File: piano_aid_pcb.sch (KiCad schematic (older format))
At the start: 15 parts

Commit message: Added screw terminal and power regulation
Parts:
- added C?: 10µ, symbol Device:CP1
- added C?: 22µ, symbol Device:CP1
- added J?: Screw_Terminal_01x02, symbol Connector:Screw_Terminal_01x02
- added U?: AZ1117-3.3, symbol Regulator_Linear:AZ1117-3.3
- C?: value CP1 -> 1000µ
- U?: symbol 317030213:317030213 -> piano_aid_pcb-rescue:317030213-317030213
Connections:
- net 3.3V: now also C?.1, U?.2 (VO)
- net 5V: now also J?.1 (Pin_1)
- net GND: now also C?.1, C?.2, C?.2, J?.2 (Pin_2), U?.1 (GND), U?.3 (VI)
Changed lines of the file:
@@
 $EndDescr
 $Comp
-L 317030213:317030213 U?
+L piano_aid_pcb-rescue:317030213-317030213 U?
 U 1 1 6137BBB1
 P 4650 3700
@@
 P 1650 1000
 F 0 "C?" H 1765 1046 50  0000 L CNN
-F 1 "CP1" H 1765 955 50  0000 L CNN
+F 1 "1000µ" H 1765 955 50  0000 L CNN
 F 2 "" H 1650 1000 50  0001 C CNN
 F 3 "~" H 1650 1000 50  0001 C CNN
@@
 Wire Wire Line
 	1200 3100 2000 3100
-Text GLabel 2300 850  2    50   Input ~ 0
+Text GLabel 3000 850  2    50   Input ~ 0
 5V
-Text GLabel 2300 1150 2    50   Input ~ 0
-GND
-Wire Wire Line
-	1650 1150 2300 1150
+Text GLabel 3000 1150 2    50   Input ~ 0
+GND
 Connection ~ 1650 1150
-Wire Wire Line
-	1650 850  2300 850
 Connection ~ 1650 850
 Text GLabel 9250 800  1    50   Input ~ 0
@@
 Wire Wire Line
 	8300 4500 8900 4500
+$Comp
+L Regulator_Linear:AZ1117-3.3 U?
+U 1 1 6144F069
+P 1800 2050
+F 0 "U?" H 1800 2199 50  0000 C CNN
+F 1 "AZ1117-3.3" H 1800 2290 50  0000 C CNN
+F 2 "" H 1800 2300 50  0001 C CIN
+F 3 "https://www.diodes.com/assets/Datasheets/AZ1117.pdf" H 1800 2050 50  0001 C CNN
+	1    1800 2050
+	-1   0    0    1
+$EndComp
+Wire Wire Line
+	1650 1150 1800 1150
+Connection ~ 1800 1150
+Wire Wire Line
+	1800 1150 2100 1150
+Connection ~ 2100 1150
+$Comp
+L Device:CP1 C?
+U 1 1 61457074
+P 1950 1550
+F 0 "C?" V 1698 1550 50  0000 C CNN
+F 1 "10µ" V 1789 1550 50  0000 C CNN
+F 2 "" H 1950 1550 50  0001 C CNN
+F 3 "~" H 1950 1550 50  0001 C CNN
+	1    1950 1550
+	0    1    1    0
+$EndComp
+$Comp
+L Device:CP1 C?
+U 1 1 6145E06D
+P 1650 1550
+F 0 "C?" V 1902 1550 50  0000 C CNN
+F 1 "22µ" V 1811 1550 50  0000 C CNN
+F 2 "" H 1650 1550 50  0001 C CNN
+F 3 "~" H 1650 1550 50  0001 C CNN
+	1    1650 1550
+	0    -1   -1   0
+$EndComp
+Connection ~ 2100 1550
+Wire Wire Line
+	2100 1550 2100 2050
+Connection ~ 1800 1550
+Wire Wire Line
+	1800 1550 1800 1750
+Wire Wire Line
+	1500 1550 1500 2050
+Wire Wire Line
+	2100 1150 2100 1550
+Wire Wire Line
+	1800 1150 1800 1550
+Wire Wire Line
+	1500 1550 1200 1550
+Connection ~ 1500 1550
+Text GLabel 1200 1550 0    50   Input ~ 0
+3.3V
+$Comp
+L Connector:Screw_Terminal_01x02 J?
+U 1 1 61467FBD
+P 2600 600
+F 0 "J?" V 2564 412 50  0000 R CNN
+F 1 "Screw_Terminal_01x02" V 2473 412 50  0000 R CNN
+F 2 "" H 2600 600 50  0001 C CNN
+F 3 "~" H 2600 600 50  0001 C CNN
+	1    2600 600
+	0    -1   -1   0
+$EndComp
+Wire Wire Line
+	2600 850  2600 800
+Wire Wire Line
+	1650 850  2600 850
+Wire Wire Line
+	2600 850  3000 850
+Connection ~ 2600 850
+Wire Wire Line
+	2700 800  2700 1150
+Wire Wire Line
+	2700 1150 3000 1150
+Wire Wire Line
+	2100 1150 2700 1150
+Connection ~ 2700 1150
 $EndSCHEMATC

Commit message: Added more connections
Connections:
- net GND: now also U?.1
- net MIDI_DIN: now reaches U?.21 (P0.08)
- net MIDI_DIN: now also R?.2, U?.6 (VO2)
- net at U?.31 (P0.17): now also U?.2
- net at U?.4: now also R?.2
- net LED_DIN: now reaches R?.1
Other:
- moved on the sheet: R?, U?
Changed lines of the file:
@@
 L 74xGxx:74AHCT1G125 U?
 U 1 1 6138B78A
-P 1050 6300
-F 0 "U?" H 1025 6125 50  0000 C CNN
-F 1 "74AHCT1G125" H 1025 6034 50  0000 C CNN
-F 2 "" H 1050 6300 50  0001 C CNN
-F 3 "http://www.ti.com/lit/sg/scyt129e/scyt129e.pdf" H 1050 6300 50  0001 C CNN
-	1    1050 6300
+P 7950 2800
+F 0 "U?" H 7925 2625 50  0000 C CNN
+F 1 "74AHCT1G125" H 7925 2534 50  0000 C CNN
+F 2 "" H 7950 2800 50  0001 C CNN
+F 3 "http://www.ti.com/lit/sg/scyt129e/scyt129e.pdf" H 7950 2800 50  0001 C CNN
+	1    7950 2800
 	1    0    0    -1
 $EndComp
@@
 L Device:R R?
 U 1 1 6139F900
-P 1650 6300
-F 0 "R?" V 1443 6300 50  0000 C CNN
-F 1 "440" V 1534 6300 50  0000 C CNN
-F 2 "" V 1580 6300 50  0001 C CNN
-F 3 "~" H 1650 6300 50  0001 C CNN
-	1    1650 6300
+P 8550 2800
+F 0 "R?" V 8343 2800 50  0000 C CNN
+F 1 "440" V 8434 2800 50  0000 C CNN
+F 2 "" V 8480 2800 50  0001 C CNN
+F 3 "~" H 8550 2800 50  0001 C CNN
+	1    8550 2800
 	0    1    1    0
 $EndComp
@@
 Wire Wire Line
 	5650 3700 6900 3700
-Wire Wire Line
-	6900 3700 6900 5150
 $Comp
 L Connector:Conn_01x06_Female J?
@@
 	-1   0    0    1
 $EndComp
-Wire Wire Line
-	2500 3300 1200 3300
-Wire Wire Line
-	2500 3300 2500 5150
 Text Label 1250 2800 0    50   ~ 0
 VDD
@@
 	9250 4300 9150 4300
 Wire Wire Line
-	2500 5150 6900 5150
-Wire Wire Line
 	8650 4000 9250 4000
 Wire Wire Line
@@
 	2100 1150 2700 1150
 Connection ~ 2700 1150
+Text GLabel 7950 2400 1    50   Input ~ 0
+GND
+Wire Wire Line
+	7950 2600 7950 2400
+Wire Wire Line
+	5650 3300 6900 3300
+Wire Wire Line
+	6900 3300 6900 2800
+Wire Wire Line
+	6900 2800 7650 2800
+Wire Wire Line
+	8200 2800 8400 2800
+Wire Wire Line
+	8700 2800 9250 2800
+Text GLabel 9250 2800 2    50   Input ~ 0
+LED_DIN
+Text GLabel 6900 3700 2    50   Input ~ 0
+RESET
+Text GLabel 2000 3300 2    50   Input ~ 0
+RESET
+Wire Wire Line
+	1200 3300 2000 3300
+Text GLabel 10100 1450 2    50   Input ~ 0
+MIDI_DIN
+Text GLabel 3150 4000 0    50   Input ~ 0
+MIDI_DIN
+Wire Wire Line
+	3150 4000 3650 4000
 $EndSCHEMATC

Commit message: Added more caps
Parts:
- added C?: 0.1µ, symbol Device:CP1
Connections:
- net 5V: now also C?.1
- net GND: now also C?.2
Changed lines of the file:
@@
 	2600 850  2600 800
 Wire Wire Line
-	1650 850  2600 850
+	1650 850  2250 850
 Wire Wire Line
 	2600 850  3000 850
@@
 	2700 1150 3000 1150
 Wire Wire Line
-	2100 1150 2700 1150
+	2100 1150 2250 1150
 Connection ~ 2700 1150
 Text GLabel 7950 2400 1    50   Input ~ 0
@@
 Wire Wire Line
 	3150 4000 3650 4000
+$Comp
+L Device:CP1 C?
+U 1 1 61480AF3
+P 2250 1000
+F 0 "C?" H 2365 1046 50  0000 L CNN
+F 1 "0.1µ" H 2365 955 50  0000 L CNN
+F 2 "" H 2250 1000 50  0001 C CNN
+F 3 "~" H 2250 1000 50  0001 C CNN
+	1    2250 1000
+	1    0    0    -1
+$EndComp
+Connection ~ 2250 850
+Wire Wire Line
+	2250 850  2600 850
+Connection ~ 2250 1150
+Wire Wire Line
+	2250 1150 2700 1150
 $EndSCHEMATC

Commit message: Added power supply to logic level converter
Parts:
- added C?: 0.1µ, symbol Device:CP1
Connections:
- net 5V is gone; now on net VCC: C?.1, C?.1, C?.1, J?.1, J?.1 (Pin_1), U?.8 (VCC)
- net GND: now also C?.2
- net at J?.2: now also C?.1
- no-connect marks 5 -> 4
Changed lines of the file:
@@
 NoConn ~ 6600 1000
 NoConn ~ 6600 1900
-NoConn ~ 7050 1450
-Wire Wire Line
-	6900 1450 7050 1450
 Wire Wire Line
 	6600 1150 6600 1000
@@
 Wire Wire Line
 	2250 1150 2700 1150
+Wire Wire Line
+	7250 1450 7250 1750
+Wire Wire Line
+	6900 1450 7250 1450
+$Comp
+L Device:CP1 C?
+U 1 1 6148405B
+P 7250 1900
+F 0 "C?" H 7365 1946 50  0000 L CNN
+F 1 "0.1µ" H 7365 1855 50  0000 L CNN
+F 2 "" H 7250 1900 50  0001 C CNN
+F 3 "~" H 7250 1900 50  0001 C CNN
+	1    7250 1900
+	1    0    0    -1
+$EndComp
+Text GLabel 7250 2050 3    50   Input ~ 0
+GND
+Wire Wire Line
+	8000 2850 8000 2950
+Wire Wire Line
+	8000 2950 8300 2950
+Wire Wire Line
+	8300 2950 8300 3250
+Wire Wire Line
+	8000 2750 8000 2650
+Wire Wire Line
+	8000 2650 8300 2650
+Wire Wire Line
+	8300 2650 8300 2400
+Text GLabel 8300 3250 3    50   Input ~ 0
+GND
+Text GLabel 8300 2400 1    50   Input ~ 0
+5V
 $EndSCHEMATC

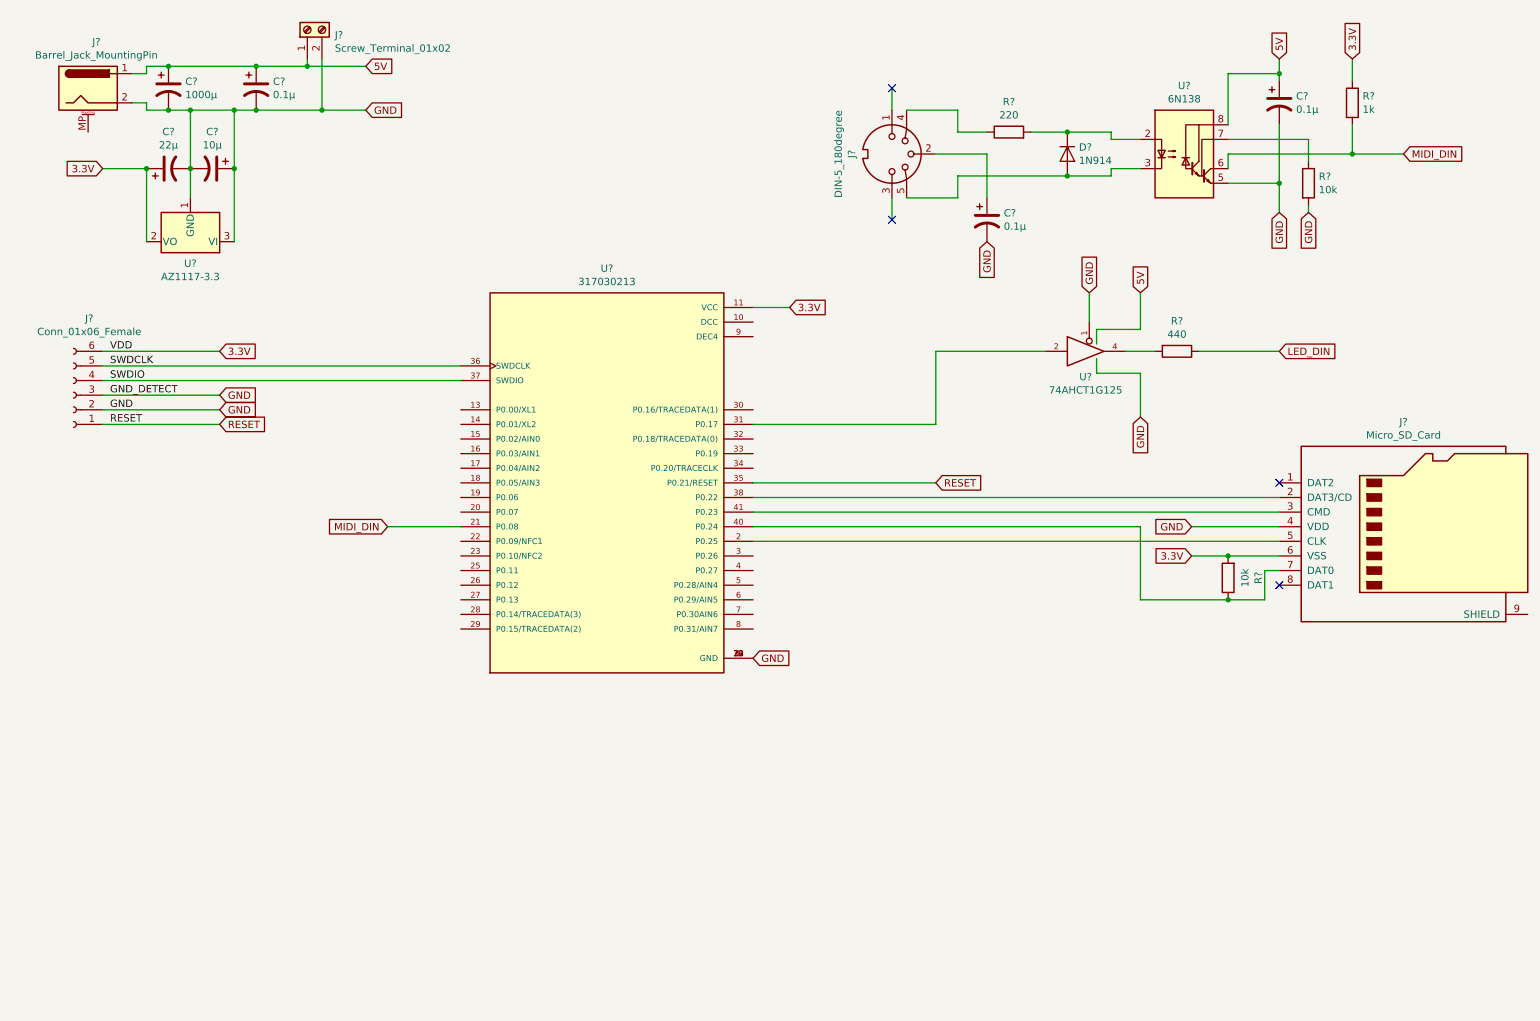
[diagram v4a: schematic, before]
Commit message: Updated MIDI-DIN
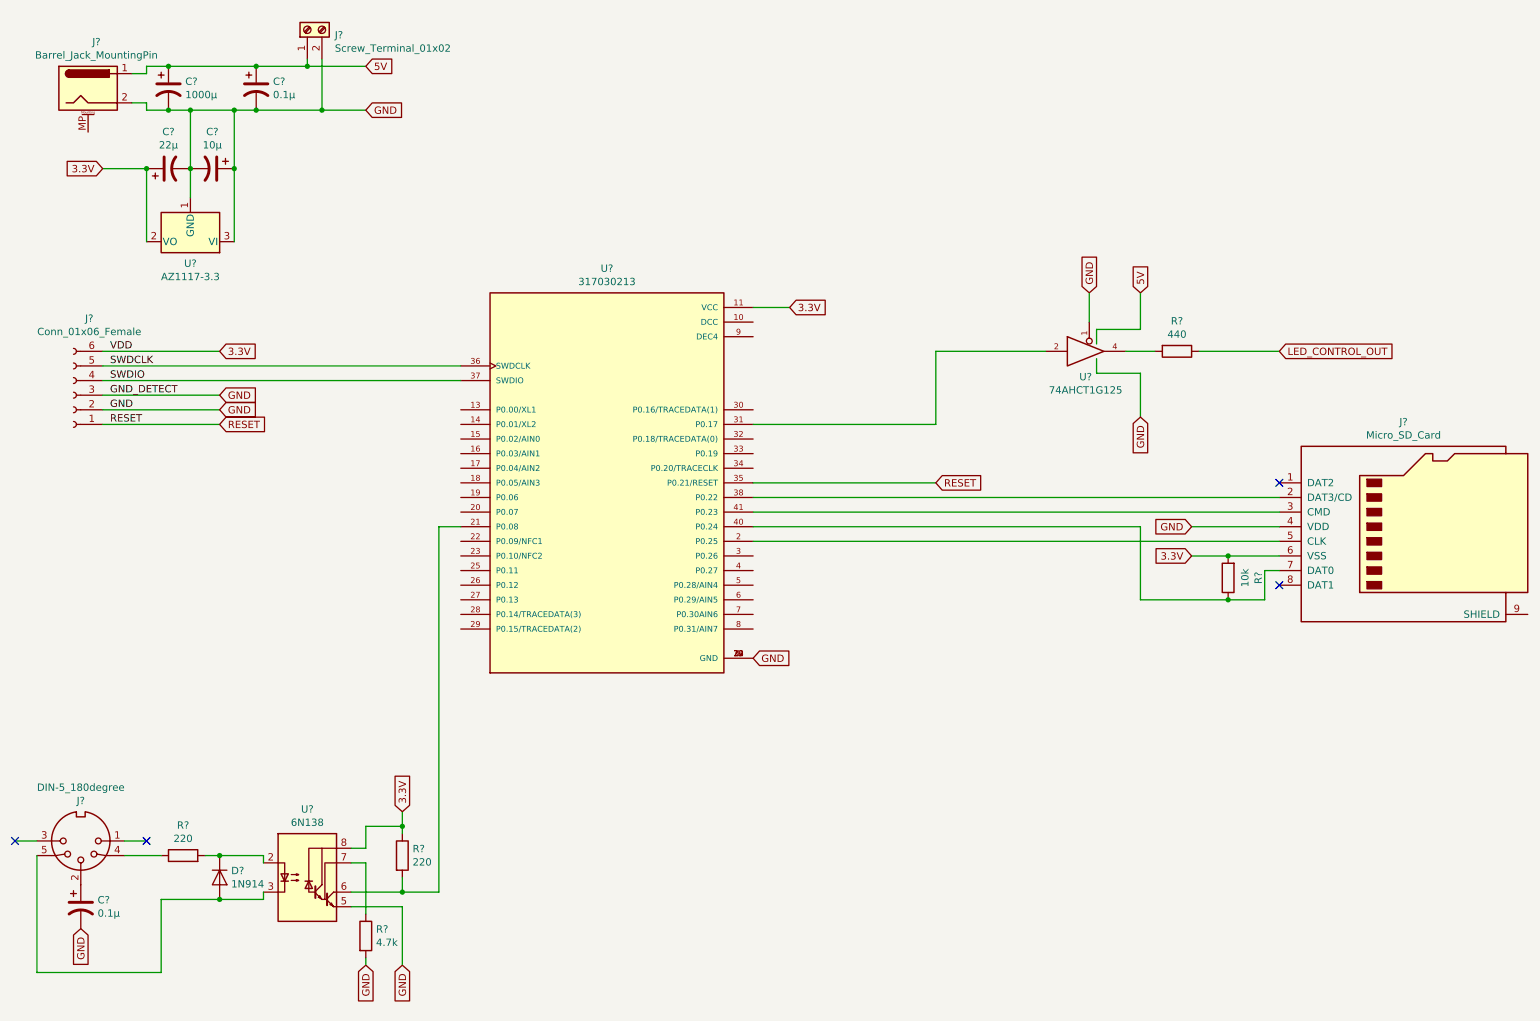
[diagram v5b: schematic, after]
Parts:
- removed C?: 0.1µ, symbol Device:CP1
- removed R?: 1k, symbol Device:R
- added R?: 220, symbol Device:R
- R?: value 10k -> 4.7k
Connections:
- net 3.3V: now also U?.8 (VCC), R?.1
- net VCC: no longer U?.8 (VCC)
- net LED_DIN renamed LED_CONTROL_OUT
- net MIDI_DIN: no longer names the net of U?.21 (P0.08), U?.6 (VO2)
- net MIDI_DIN: now also R?.2
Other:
- moved on the sheet: C?, D?, J?, R?, U?
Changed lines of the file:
@@
-$EndComp
-$Comp
-L Connector:DIN-5_180degree J?
-U 1 1 61399AC9
-P 6600 1450
-F 0 "J?" H 6600 1175 50  0000 C CNN
-F 1 "DIN-5_180degree" H 6600 1084 50  0000 C CNN
-F 2 "" H 6600 1450 50  0001 C CNN
-F 3 "http://www.mouser.com/ds/2/18/40_c091_abd_e-75918.pdf" H 6600 1450 50  0001 C CNN
-	1    6600 1450
-	0    1    1    0
 $EndComp
 $Comp
@@
 Wire Wire Line
 	1500 1150 1650 1150
-$Comp
-L Diode:1N914 D?
-U 1 1 613A3625
-P 7800 1450
-F 0 "D?" V 7754 1529 50  0000 L CNN
-F 1 "1N914" V 7845 1529 50  0000 L CNN
-F 2 "Diode_THT:D_DO-35_SOD27_P7.62mm_Horizontal" H 7800 1275 50  0001 C CNN
-F 3 "http://www.vishay.com/docs/85622/1n914.pdf" H 7800 1450 50  0001 C CNN
-	1    7800 1450
-	0    1    1    0
-$EndComp
-$Comp
-L Device:R R?
-U 1 1 613ABD6D
-P 7400 1300
-F 0 "R?" V 7607 1300 50  0000 C CNN
-F 1 "220" V 7516 1300 50  0000 C CNN
-F 2 "" V 7330 1300 50  0001 C CNN
-F 3 "~" H 7400 1300 50  0001 C CNN
-	1    7400 1300
-	0    -1   -1   0
-$EndComp
-$Comp
-L Isolator:6N138 U?
-U 1 1 613CE47C
-P 8600 1450
-F 0 "U?" H 8600 1917 50  0000 C CNN
-F 1 "6N138" H 8600 1826 50  0000 C CNN
-F 2 "" H 8890 1150 50  0001 C CNN
-F 3 "http://www.onsemi.com/pub/Collateral/HCPL2731-D.pdf" H 8890 1150 50  0001 C CNN
-	1    8600 1450
-	1    0    0    -1
-$EndComp
 Wire Wire Line
 	1200 2900 3650 2900
@@
 $EndComp
 Wire Wire Line
-	6700 1150 7050 1150
-Wire Wire Line
-	7050 1150 7050 1300
-Wire Wire Line
-	7050 1300 7250 1300
-Wire Wire Line
-	7550 1300 7800 1300
-Wire Wire Line
-	7800 1300 8100 1300
-Wire Wire Line
-	8100 1300 8100 1350
-Wire Wire Line
-	8100 1350 8300 1350
-Connection ~ 7800 1300
-Wire Wire Line
-	7800 1600 8100 1600
-Wire Wire Line
-	8100 1600 8100 1550
-Wire Wire Line
-	8100 1550 8300 1550
-Wire Wire Line
-	6700 1750 7050 1750
-Wire Wire Line
-	7050 1750 7050 1600
-Wire Wire Line
-	7050 1600 7800 1600
-Connection ~ 7800 1600
-$Comp
-L Device:CP1 C?
-U 1 1 6142C582
-P 9250 1100
-F 0 "C?" H 9365 1146 50  0000 L CNN
-F 1 "0.1µ" H 9365 1055 50  0000 L CNN
-F 2 "" H 9250 1100 50  0001 C CNN
-F 3 "~" H 9250 1100 50  0001 C CNN
-	1    9250 1100
-	1    0    0    -1
-$EndComp
-Wire Wire Line
-	8900 1250 8900 900
-Wire Wire Line
-	8900 900  9250 900
-Wire Wire Line
-	9250 900  9250 800
-Wire Wire Line
-	9250 950  9250 900
-Connection ~ 9250 900
-Wire Wire Line
-	8900 1650 9250 1650
-Wire Wire Line
-	9250 1650 9250 1250
-Wire Wire Line
-	9250 1850 9250 1650
-Connection ~ 9250 1650
-$Comp
-L Device:R R?
-U 1 1 61445BFE
-P 9450 1650
-F 0 "R?" H 9520 1696 50  0000 L CNN
-F 1 "10k" H 9520 1605 50  0000 L CNN
-F 2 "" V 9380 1650 50  0001 C CNN
-F 3 "~" H 9450 1650 50  0001 C CNN
-	1    9450 1650
-	1    0    0    -1
-$EndComp
-Wire Wire Line
-	9450 1800 9450 1850
-Wire Wire Line
-	8900 1350 9450 1350
-Wire Wire Line
-	9450 1350 9450 1500
-Wire Wire Line
-	8900 1550 8900 1450
-Wire Wire Line
-	8900 1450 9750 1450
-$Comp
-L Device:R R?
-U 1 1 6144C0EE
-P 9750 1100
-F 0 "R?" H 9820 1146 50  0000 L CNN
-F 1 "1k" H 9820 1055 50  0000 L CNN
-F 2 "" V 9680 1100 50  0001 C CNN
-F 3 "~" H 9750 1100 50  0001 C CNN
-	1    9750 1100
-	1    0    0    -1
-$EndComp
-Wire Wire Line
-	9750 800  9750 950
-Wire Wire Line
-	9750 1250 9750 1450
-Connection ~ 9750 1450
-Wire Wire Line
-	9750 1450 10100 1450
-Wire Wire Line
 	1200 3100 2000 3100
 Text GLabel 3000 850  2    50   Input ~ 0
@@
 Connection ~ 1650 1150
 Connection ~ 1650 850
-Text GLabel 9250 800  1    50   Input ~ 0
-5V
-Text GLabel 9750 800  1    50   Input ~ 0
-3.3V
-Text GLabel 9250 1850 3    50   Input ~ 0
-GND
-Text GLabel 9450 1850 3    50   Input ~ 0
-GND
 Text GLabel 8650 4200 0    50   Input ~ 0
 3.3V
@@
 	8650 4200 8900 4200
 Connection ~ 8900 4200
-NoConn ~ 6600 1000
-NoConn ~ 6600 1900
-Wire Wire Line
-	6600 1150 6600 1000
-Wire Wire Line
-	6600 1750 6600 1900
 Wire Wire Line
 	9250 3800 5650 3800
@@
 	2100 1150 2250 1150
 Connection ~ 2700 1150
-Text GLabel 7950 2400 1    50   Input ~ 0
-GND
 Wire Wire Line
 	7950 2600 7950 2400
@@
 	8700 2800 9250 2800
 Text GLabel 9250 2800 2    50   Input ~ 0
-LED_DIN
+LED_CONTROL_OUT
 Text GLabel 6900 3700 2    50   Input ~ 0
 RESET
@@
 Wire Wire Line
 	1200 3300 2000 3300
-Text GLabel 10100 1450 2    50   Input ~ 0
-MIDI_DIN
-Text GLabel 3150 4000 0    50   Input ~ 0
-MIDI_DIN
-Wire Wire Line
-	3150 4000 3650 4000
 $Comp
 L Device:CP1 C?
@@
 	2250 1150 2700 1150
 Wire Wire Line
-	7250 1450 7250 1750
-Wire Wire Line
-	6900 1450 7250 1450
+	8000 2850 8000 2950
+Wire Wire Line
+	8000 2950 8300 2950
+Wire Wire Line
+	8300 2950 8300 3250
+Wire Wire Line
+	8000 2750 8000 2650
+Wire Wire Line
+	8000 2650 8300 2650
+Wire Wire Line
+	8300 2650 8300 2400
+Text GLabel 8300 3250 3    50   Input ~ 0
+GND
+Text GLabel 8300 2400 1    50   Input ~ 0
+5V
+Text GLabel 7950 2400 1    50   Input ~ 0
+GND
+Wire Wire Line
+	3650 4000 3500 4000
+Wire Wire Line
+	3500 4000 3500 6500
+Connection ~ 2000 6550
+Wire Wire Line
+	2000 6550 1600 6550
+Connection ~ 2000 6250
+Wire Wire Line
+	1900 6250 2000 6250
+Wire Wire Line
+	1350 6250 1600 6250
+$Comp
+L Connector:DIN-5_180degree J?
+U 1 1 61399AC9
+P 1050 6150
+F 0 "J?" H 1050 5875 50  0000 C CNN
+F 1 "DIN-5_180degree" H 1050 5784 50  0000 C CNN
+F 2 "" H 1050 6150 50  0001 C CNN
+F 3 "http://www.mouser.com/ds/2/18/40_c091_abd_e-75918.pdf" H 1050 6150 50  0001 C CNN
+	1    1050 6150
+	-1   0    0    1
+$EndComp
+$Comp
+L Diode:1N914 D?
+U 1 1 613A3625
+P 2000 6400
+F 0 "D?" V 1954 6479 50  0000 L CNN
+F 1 "1N914" V 2045 6479 50  0000 L CNN
+F 2 "Diode_THT:D_DO-35_SOD27_P7.62mm_Horizontal" H 2000 6225 50  0001 C CNN
+F 3 "http://www.vishay.com/docs/85622/1n914.pdf" H 2000 6400 50  0001 C CNN
+	1    2000 6400
+	0    1    1    0
+$EndComp
+Wire Wire Line
+	2000 6250 2300 6250
+Wire Wire Line
+	2300 6250 2300 6300
+Wire Wire Line
+	2000 6550 2300 6550
+Wire Wire Line
+	2300 6550 2300 6500
+$Comp
+L Device:R R?
+U 1 1 61445BFE
+P 3000 6800
+F 0 "R?" H 3070 6846 50  0000 L CNN
+F 1 "4.7k" H 3070 6755 50  0000 L CNN
+F 2 "" V 2930 6800 50  0001 C CNN
+F 3 "~" H 3000 6800 50  0001 C CNN
+	1    3000 6800
+	1    0    0    -1
+$EndComp
+Wire Wire Line
+	3000 6950 3000 7000
+Wire Wire Line
+	2900 6300 3000 6300
+Text GLabel 3250 5950 1    50   Input ~ 0
+3.3V
+Text GLabel 3250 7000 3    50   Input ~ 0
+GND
+Text GLabel 3000 7000 3    50   Input ~ 0
+GND
 $Comp
 L Device:CP1 C?
 U 1 1 6148405B
-P 7250 1900
-F 0 "C?" H 7365 1946 50  0000 L CNN
-F 1 "0.1µ" H 7365 1855 50  0000 L CNN
-F 2 "" H 7250 1900 50  0001 C CNN
-F 3 "~" H 7250 1900 50  0001 C CNN
-	1    7250 1900
-	1    0    0    -1
-$EndComp
-Text GLabel 7250 2050 3    50   Input ~ 0
-GND
-Wire Wire Line
-	8000 2850 8000 2950
-Wire Wire Line
-	8000 2950 8300 2950
-Wire Wire Line
-	8300 2950 8300 3250
-Wire Wire Line
-	8000 2750 8000 2650
-Wire Wire Line
-	8000 2650 8300 2650
-Wire Wire Line
-	8300 2650 8300 2400
-Text GLabel 8300 3250 3    50   Input ~ 0
-GND
-Text GLabel 8300 2400 1    50   Input ~ 0
-5V
+P 1050 6600
+F 0 "C?" H 1165 6646 50  0000 L CNN
+F 1 "0.1µ" H 1165 6555 50  0000 L CNN
+F 2 "" H 1050 6600 50  0001 C CNN
+F 3 "~" H 1050 6600 50  0001 C CNN
+	1    1050 6600
+	1    0    0    -1
+$EndComp
+Text GLabel 1050 6750 3    50   Input ~ 0
+GND
+$Comp
+L Device:R R?
+U 1 1 613ABD6D
+P 1750 6250
+F 0 "R?" V 1957 6250 50  0000 C CNN
+F 1 "220" V 1866 6250 50  0000 C CNN
+F 2 "" V 1680 6250 50  0001 C CNN
+F 3 "~" H 1750 6250 50  0001 C CNN
+	1    1750 6250
+	0    -1   -1   0
+$EndComp
+Wire Wire Line
+	750  6250 750  7050
+Wire Wire Line
+	750  7050 1600 7050
+Wire Wire Line
+	1600 7050 1600 6550
+Wire Wire Line
+	750  6150 600  6150
+Wire Wire Line
+	1350 6150 1500 6150
+NoConn ~ 600  6150
+NoConn ~ 1500 6150
+$Comp
+L Device:R R?
+U 1 1 614B717D
+P 3250 6250
+F 0 "R?" H 3320 6296 50  0000 L CNN
+F 1 "220" H 3320 6205 50  0000 L CNN
+F 2 "" V 3180 6250 50  0001 C CNN
+F 3 "~" H 3250 6250 50  0001 C CNN
+	1    3250 6250
+	1    0    0    -1
+$EndComp
+$Comp
+L Isolator:6N138 U?
+U 1 1 613CE47C
+P 2600 6400
+F 0 "U?" H 2600 6867 50  0000 C CNN
+F 1 "6N138" H 2600 6776 50  0000 C CNN
+F 2 "" H 2890 6100 50  0001 C CNN
+F 3 "http://www.onsemi.com/pub/Collateral/HCPL2731-D.pdf" H 2890 6100 50  0001 C CNN
+	1    2600 6400
+	1    0    0    -1
+$EndComp
+Wire Wire Line
+	2900 6200 3000 6200
+Wire Wire Line
+	3000 6200 3000 6050
+Wire Wire Line
+	2900 6500 3250 6500
+Wire Wire Line
+	3250 5950 3250 6050
+Wire Wire Line
+	3250 6400 3250 6500
+Connection ~ 3250 6500
+Wire Wire Line
+	3250 6050 3000 6050
+Connection ~ 3250 6050
+Wire Wire Line
+	3250 6050 3250 6100
+Wire Wire Line
+	3250 6500 3500 6500
+Wire Wire Line
+	3000 6300 3000 6650
+Wire Wire Line
+	2900 6600 3250 6600
+Wire Wire Line
+	3250 6600 3250 7000
 $EndSCHEMATC
